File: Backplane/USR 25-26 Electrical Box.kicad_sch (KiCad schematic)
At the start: 3 parts

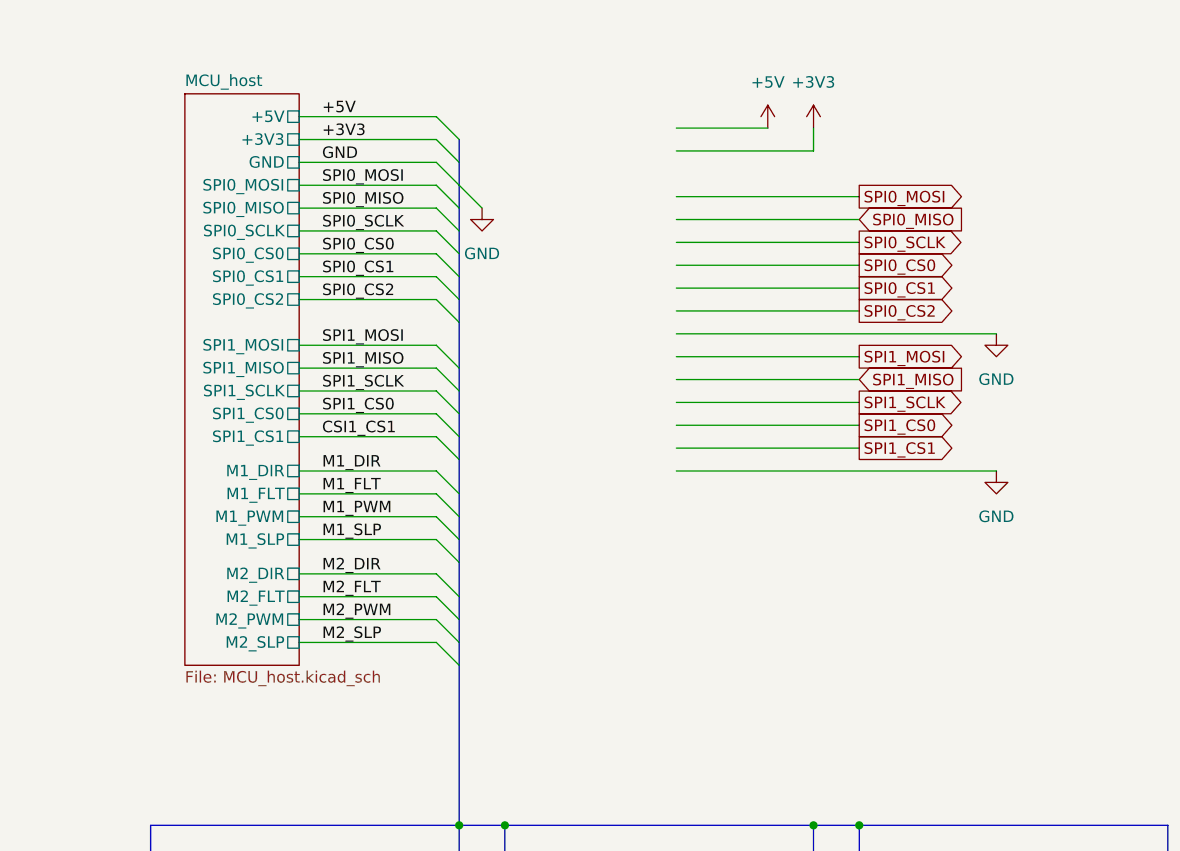
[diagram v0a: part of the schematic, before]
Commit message: Reorganized directory tree
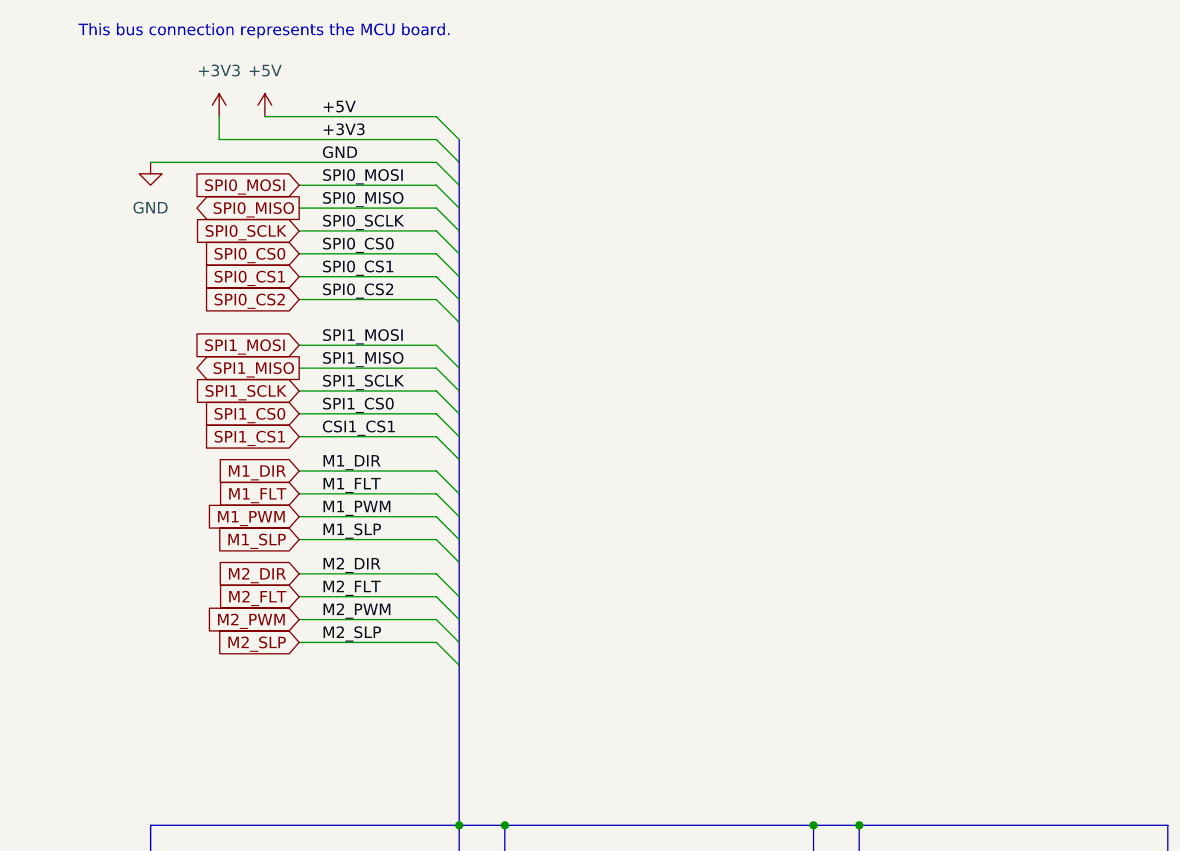
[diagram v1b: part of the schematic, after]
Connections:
- net CSI1_CS1 is gone; now on net SPI1_CS1: J1.46, J2.46, J3.46
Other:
- removed sheet MCU_host
- note added: "This bus connection represents the MCU board."

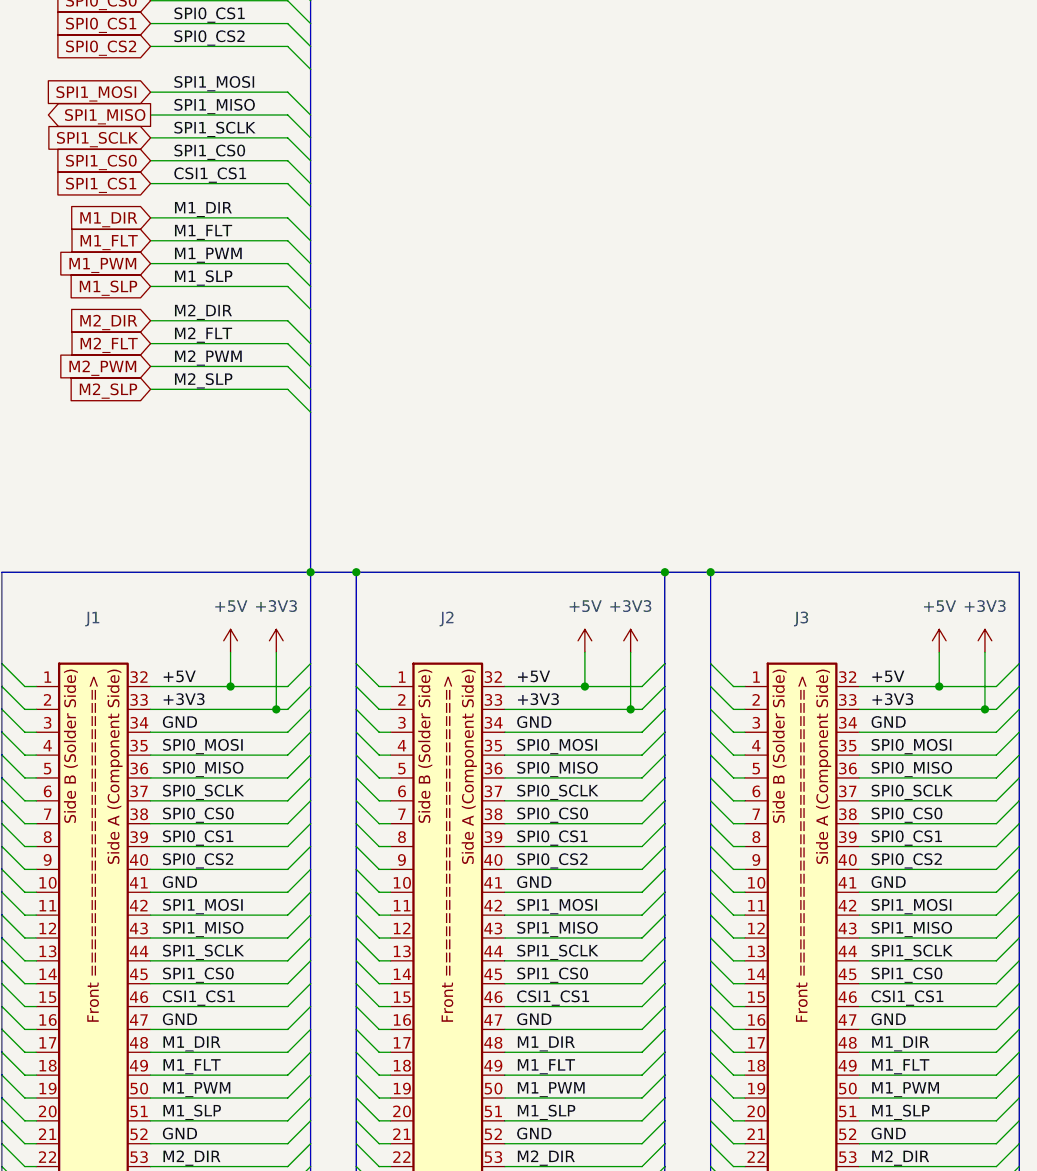
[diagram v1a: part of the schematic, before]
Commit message: Begin work on PCB layout
PCB layout for both the bus board and the MCU card have begun.
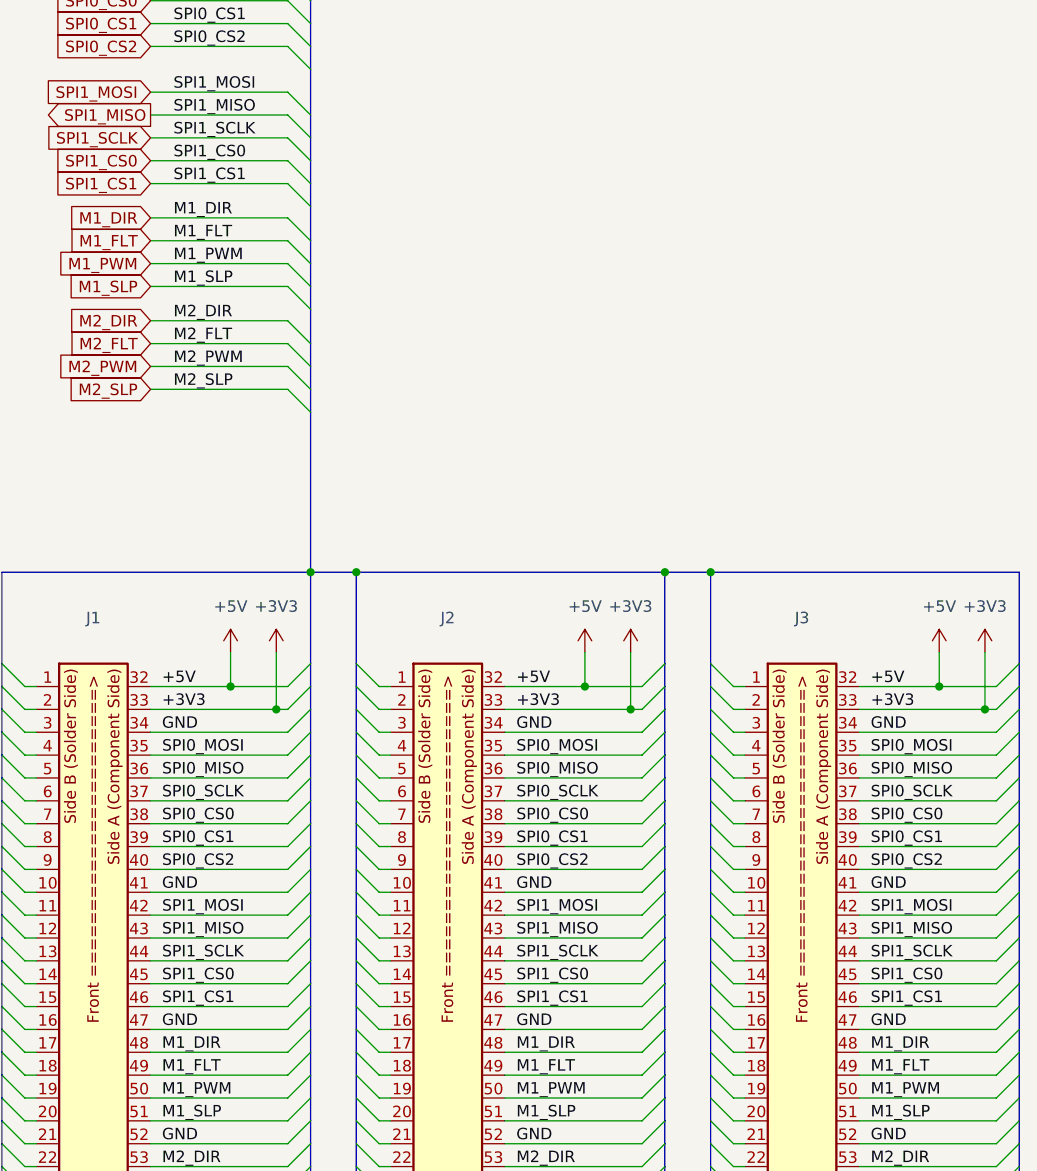
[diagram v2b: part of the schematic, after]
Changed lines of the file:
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@@
 		)
 	)
-	(label "CSI1_CS1"
+	(label "SPI1_CS1"
 		(at 87.63 153.67 0)
 		(effects
@@
 		)
 	)
-	(label "CSI1_CS1"
+	(label "SPI1_CS1"
 		(at 49.53 62.23 0)
 		(effects
@@
 		)
 	)
-	(label "CSI1_CS1"
+	(label "SPI1_CS1"
 		(at 48.26 153.67 0)
 		(effects
@@
 		)
 	)
-	(label "CSI1_CS1"
+	(label "SPI1_CS1"
 		(at 127 153.67 0)
 		(effects

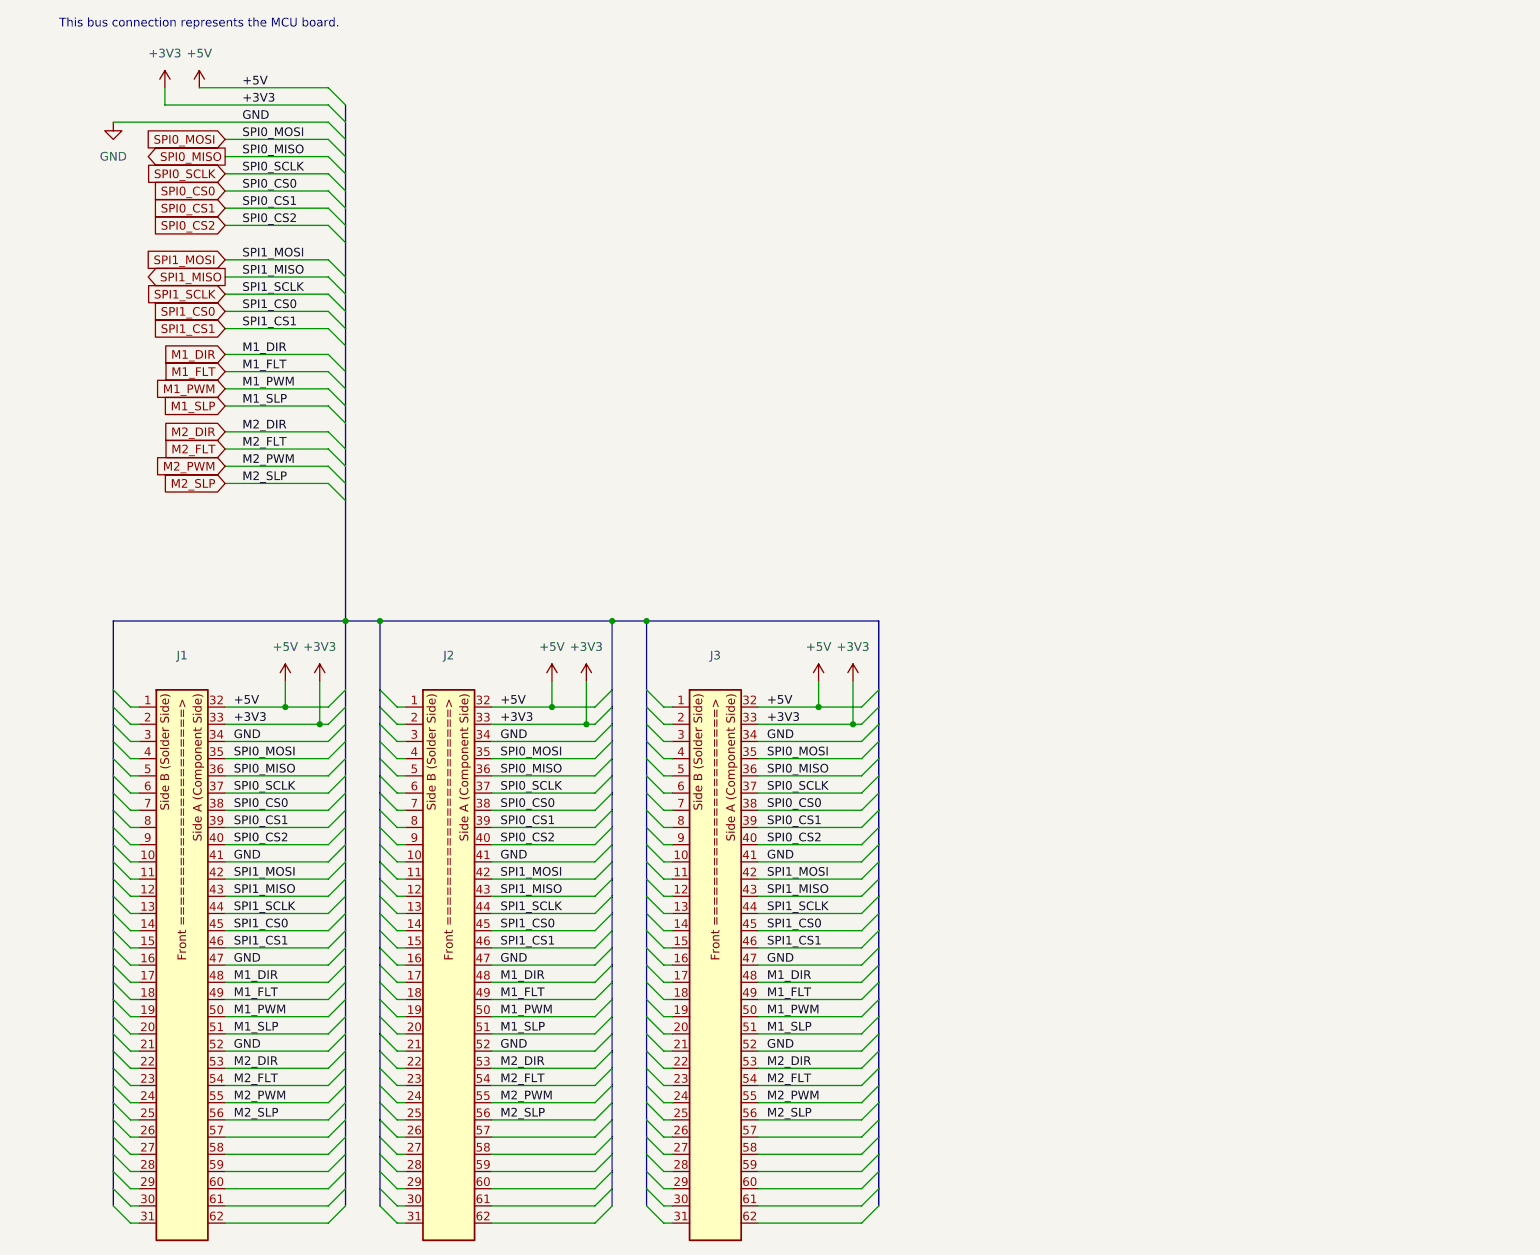
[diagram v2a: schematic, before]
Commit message: Laid out revision 0 PCB for backplane.
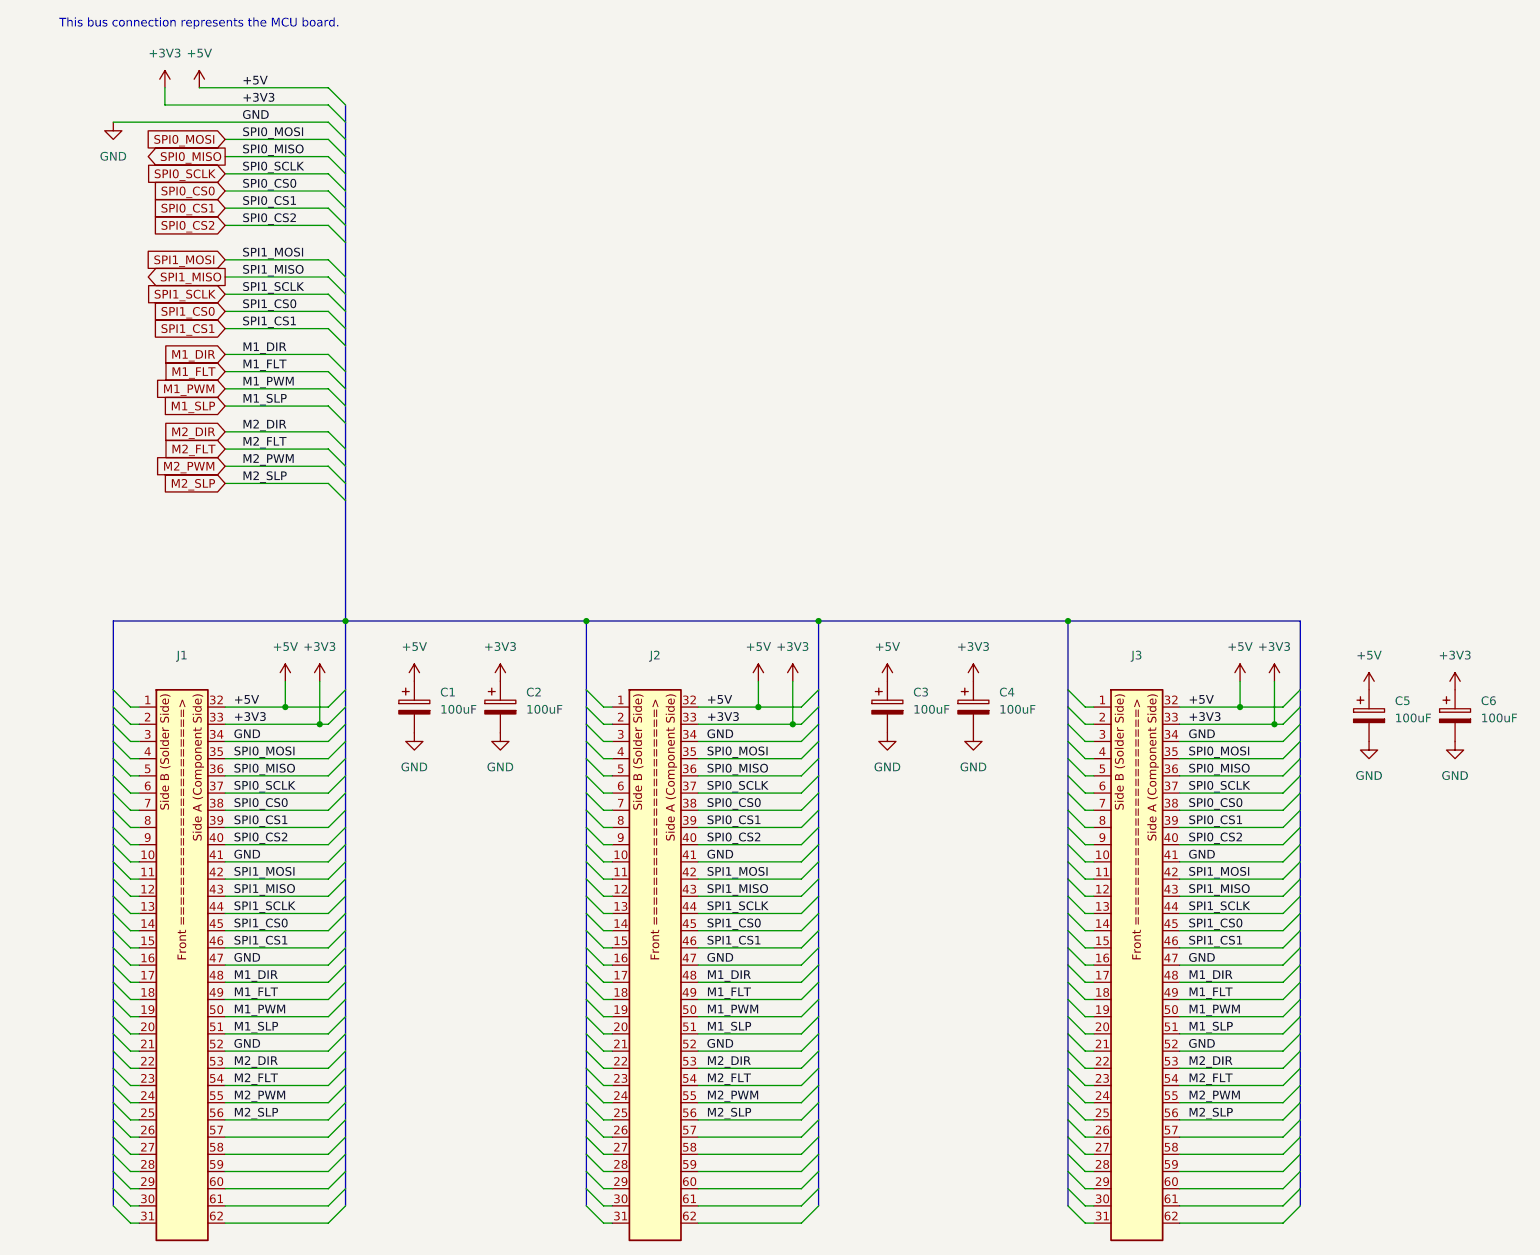
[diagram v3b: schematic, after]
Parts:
- added C1, C2, C3, C4, C5, C6: 100uF, Capacitor_THT:CP_Radial_D8.0mm_P3.50mm, symbol Device:C_Polarized
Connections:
- net +3V3: now also C2.1, C4.1, C6.1
- net +5V: now also C1.1, C3.1, C5.1
- net GND: now also C1.2, C2.2, C3.2, C4.2, C5.2, C6.2
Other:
- moved on the sheet: J2, J3
